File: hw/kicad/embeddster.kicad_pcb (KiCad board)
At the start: 2 copper layers, 1 part, among them U1 ESP32-DEVKIT-V1

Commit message: sch supporting tp1 & tp2
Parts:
- added C1: 100n, Capacitor_SMD:C_0805_2012Metric_Pad1.18x1.45mm_HandSolder, F.Cu at (63.0, 98.6)
- added C2: 100n, Capacitor_SMD:C_0805_2012Metric_Pad1.18x1.45mm_HandSolder, F.Cu at (63.0, 101.6)
- added D1: LED, LED_SMD:LED_0805_2012Metric_Pad1.15x1.40mm_HandSolder, F.Cu at (71.0, 96.7)
- added D2: LED, LED_SMD:LED_0805_2012Metric_Pad1.15x1.40mm_HandSolder, F.Cu at (71.0, 99.7)
- added D3: LED, LED_SMD:LED_0805_2012Metric_Pad1.15x1.40mm_HandSolder, F.Cu at (75.6, 81.2)
- added D4: LED, LED_SMD:LED_0805_2012Metric_Pad1.15x1.40mm_HandSolder, F.Cu at (75.6, 78.1)
- added D5: LED, LED_SMD:LED_0805_2012Metric_Pad1.15x1.40mm_HandSolder, F.Cu at (75.6, 75.1)
- added D6: LED, LED_SMD:LED_0805_2012Metric_Pad1.15x1.40mm_HandSolder, F.Cu at (75.6, 72.1)
- added J1: Conn_01x03_Pin, Connector_PinHeader_2.54mm:PinHeader_1x03_P2.54mm_Vertical, F.Cu at (68.4, 116.8)
- added J2: Conn_01x03_Pin, Connector_PinHeader_2.54mm:PinHeader_1x03_P2.54mm_Vertical, F.Cu at (73.1, 116.8)
- added J3: Conn_01x03_Pin, Connector_PinHeader_2.54mm:PinHeader_1x03_P2.54mm_Vertical, F.Cu at (77.7, 116.8)
- added J4: TP1_CONN, Connector_PinSocket_2.54mm:PinSocket_2x09_P2.54mm_Vertical, B.Cu at (104.6, 115.8)
- added JP1: Jumper_2_Open, TestPoint:TestPoint_2Pads_Pitch2.54mm_Drill0.8mm, F.Cu at (86.0, 115.5)
- added JP2: Jumper_2_Open, TestPoint:TestPoint_2Pads_Pitch2.54mm_Drill0.8mm, F.Cu at (127.8, 115.4)
- added R1: 680, Resistor_SMD:R_0805_2012Metric_Pad1.20x1.40mm_HandSolder, F.Cu at (75.7, 96.6)
- added R2: 470, Resistor_SMD:R_0805_2012Metric_Pad1.20x1.40mm_HandSolder, F.Cu at (75.7, 99.6)
- added R3: 220, Resistor_SMD:R_0805_2012Metric_Pad1.20x1.40mm_HandSolder, F.Cu at (80.3, 72.0)
- added R4: 220, Resistor_SMD:R_0805_2012Metric_Pad1.20x1.40mm_HandSolder, F.Cu at (80.3, 75.0)
- added R5: 220, Resistor_SMD:R_0805_2012Metric_Pad1.20x1.40mm_HandSolder, F.Cu at (80.3, 77.9)
- added R6: 220, Resistor_SMD:R_0805_2012Metric_Pad1.20x1.40mm_HandSolder, F.Cu at (80.3, 80.9)
- added U1: PLACA_CAN_V20190517, PLACA_CAN_V20190517:PLACA_CAN_V20190517, F.Cu at (155.5, 101.8)
- added U3: 74HC595, Package_SO:SOIC-16_3.9x9.9mm_P1.27mm, B.Cu at (95.5, 121.9)
- added U4: 74HC595, Package_SO:SOIC-16_3.9x9.9mm_P1.27mm, B.Cu at (116.3, 121.9)
- moved U2 54.9 mm to (134.6, 72.4), turned to 180 degrees
- renumbered U1 to U2
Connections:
- net Net-(U1-GND-Pad2) renamed GND
- U2 pad 1: unconnected-(U1-3V3-Pad1) -> Net-(JP2-A)
- U2 pad 10: unconnected-(U1-D19-Pad10) -> /CAN_MISO
- U2 pad 15: unconnected-(U1-D23-Pad15) -> /CAN_MOSI
- U2 pad 30: unconnected-(U1-VIN-Pad30) -> Net-(JP1-B)
- U2 pad 7: unconnected-(U1-TX2-Pad7) -> /CAN_nINT
- U2 pad 8: unconnected-(U1-D5-Pad8) -> /CAN_nCS
- U2 pad 9: unconnected-(U1-D18-Pad9) -> /CAN_SCK

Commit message: pcb ready for fab
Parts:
- added C3: 100n, Capacitor_SMD:C_0805_2012Metric_Pad1.18x1.45mm_HandSolder, F.Cu at (96.8, 46.2)
- added C4: 100n, Capacitor_SMD:C_0805_2012Metric_Pad1.18x1.45mm_HandSolder, B.Cu at (126.5, 87.1)
- added C5: 100n, Capacitor_SMD:C_0805_2012Metric_Pad1.18x1.45mm_HandSolder, B.Cu at (146.8, 86.9)
- added J5: Conn_01x05_Socket, Connector_PinSocket_2.54mm:PinSocket_1x05_P2.54mm_Vertical, B.Cu at (101.6, 100.1)
- added J6: Conn_01x05_Socket, Connector_PinSocket_2.54mm:PinSocket_1x05_P2.54mm_Vertical, B.Cu at (196.2, 48.2)
- added J7: Conn_01x05_Socket, Connector_PinSocket_2.54mm:PinSocket_1x05_P2.54mm_Vertical, B.Cu at (189.5, 89.4)
- added R7: 10k, Resistor_SMD:R_0805_2012Metric_Pad1.20x1.40mm_HandSolder, F.Cu at (120.7, 62.5)
- added R8: 10k, Resistor_SMD:R_0805_2012Metric_Pad1.20x1.40mm_HandSolder, B.Cu at (127.0, 69.6)
- D1: footprint LED_SMD:LED_0805_2012Metric_Pad1.15x1.40mm_HandSolder -> LED_THT:LED_D3.0mm
- R1: moved to B.Cu
- U3, U4: moved to F.Cu
- moved J3 76.8 mm to (108.5, 46.5), turned to 90 degrees
- moved C2 69.8 mm to (115.1, 55.1), turned to 180 degrees
- moved U3 63.8 mm to (108.8, 59.6), turned to 0 degrees
- moved D2 62.1 mm to (100.8, 45.2), turned to -45 degrees
- moved R2 57.0 mm to (92.7, 45.2), turned to -135 degrees
- moved C1 55.3 mm to (108.7, 67.6), turned to -45 degrees
- moved D1 48.5 mm to (117.6, 83.3), turned to 180 degrees
- moved J4 48.2 mm to (98.0, 68.1), turned to 0 degrees
- moved R1 46.9 mm to (120.7, 83.1), turned to -90 degrees
- moved U4 45.2 mm to (108.6, 77.3), turned to 0 degrees
- moved J2 43.8 mm to (105.9, 87.9), turned to 90 degrees
- moved JP1 39.8 mm to (115.1, 88.4)
- moved J1 30.3 mm to (89.6, 95.2), turned to 45 degrees
- moved JP2 23.1 mm to (117.6, 94.7), turned to 180 degrees
- moved D6 22.2 mm to (97.0, 78.0)
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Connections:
- U1 pad 2: unconnected-(U1-VIO-Pad2) -> +3V3
- U2 pad 11: unconnected-(U2-D21-Pad11) -> /TP1_RCHB
- U2 pad 14: unconnected-(U2-D22-Pad14) -> /TP1_RSWITCH
- U2 pad 21: unconnected-(U2-D32-Pad21) -> /595_SI
- U2 pad 22: unconnected-(U2-D33-Pad22) -> /595_LATCH_CLK
- U2 pad 23: unconnected-(U2-D25-Pad23) -> /595_nOE
- U2 pad 24: unconnected-(U2-D26-Pad24) -> /595_nRST
- U2 pad 25: unconnected-(U2-D27-Pad25) -> /595_SHIFT_CLK
- U2 pad 6: unconnected-(U2-RX2-Pad6) -> /TP1_RCHA
- U3 pad 1: /TP1_CSEGB -> /TP1_CSEGG
- U3 pad 15: /TP1_CSEGA -> /TP1_CSEGDP
- U3 pad 2: /TP1_CSEGC -> /TP1_CSEGF
- U3 pad 3: /TP1_CSEGD -> /TP1_CSEGE
- U3 pad 4: /TP1_CSEGE -> /TP1_CSEGD
- U3 pad 5: /TP1_CSEGF -> /TP1_CSEGC
- U3 pad 6: /TP1_CSEGG -> /TP1_CSEGB
- U3 pad 7: /TP1_CSEGDP -> /TP1_CSEGA
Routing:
- net +3V3: track 0.00 -> 233.9 mm, vias 0 -> 5
- net GND: track 0.00 -> 147.3 mm, vias 0 -> 8
- net /TP1_RCHB: track 0.00 -> 132.8 mm, vias 0 -> 3
- net +5V: track 0.00 -> 112.3 mm
- net /CAN_nCS: track 0.00 -> 101.3 mm
- net /TP1_RCHA: track 0.00 -> 98.5 mm, vias 0 -> 2
- net /TP1_RSWITCH: track 0.00 -> 96.0 mm, vias 0 -> 3
- net /CAN_MISO: track 0.00 -> 86.9 mm
- net /CAN_MOSI: track 0.00 -> 61.4 mm
- net /CAN_SCK: track 0.00 -> 51.5 mm
- net /595_LATCH_CLK: track 0.00 -> 51.3 mm, vias 0 -> 2
- net /595_SHIFT_CLK: track 0.00 -> 47.2 mm, vias 0 -> 1
- net /595_nRST: track 0.00 -> 46.5 mm, vias 0 -> 1
- net /CAN_nINT: track 0.00 -> 46.0 mm
- net /TP1_STATUS1: track 0.00 -> 39.7 mm
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- added copper zone on B.Cu, net GND
- added copper zone on F.Cu, net GND
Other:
- board outline added: 117.3 x 63 mm

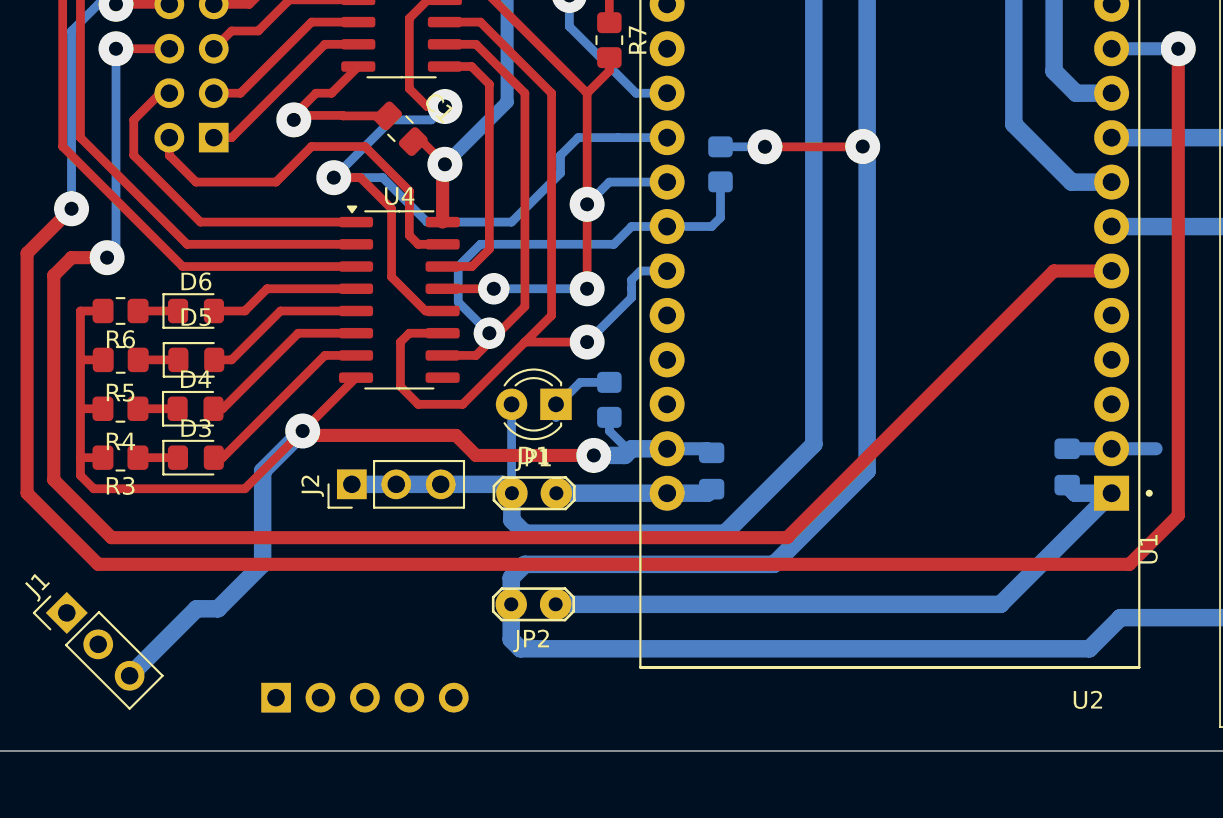
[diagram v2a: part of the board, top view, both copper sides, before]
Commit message: Add 4th quantum standoff to PCB, ground plane adjustments
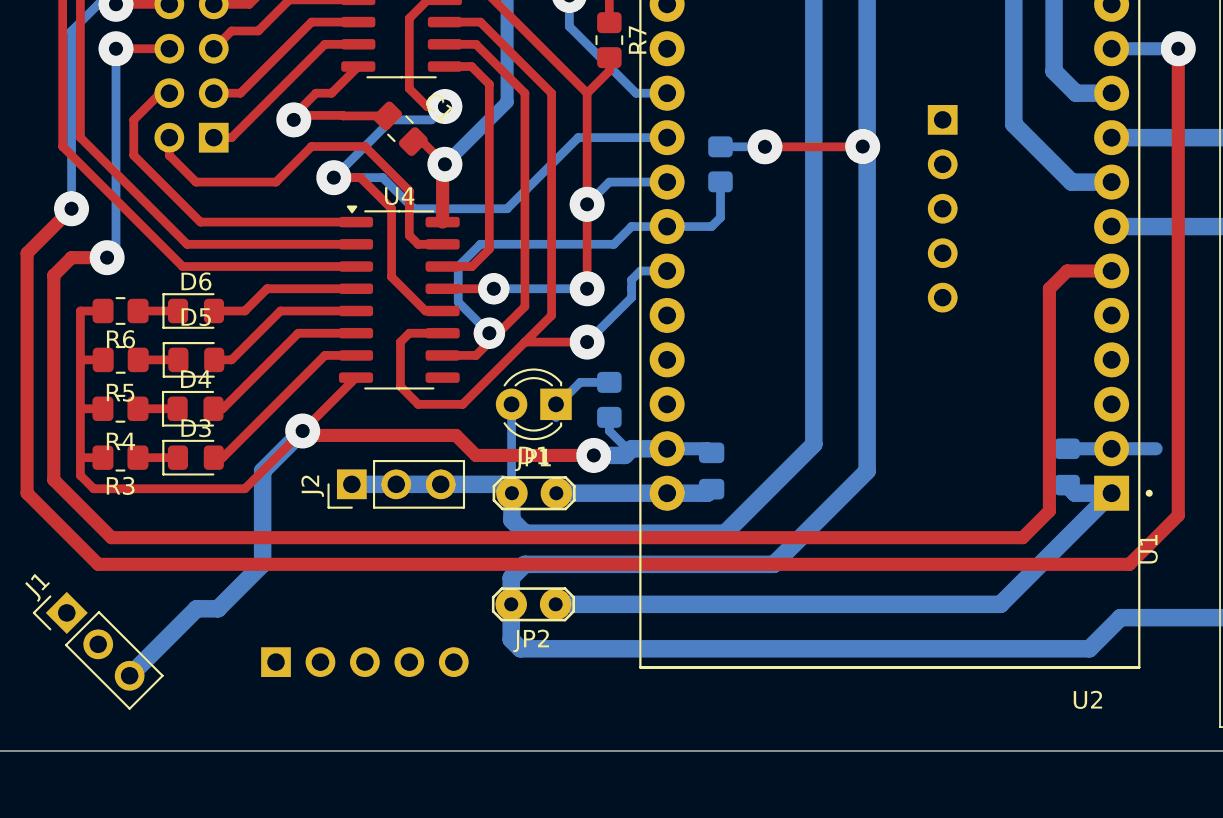
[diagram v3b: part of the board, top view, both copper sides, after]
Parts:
- added J8: Conn_01x05_Socket, Connector_PinSocket_2.54mm:PinSocket_1x05_P2.54mm_Vertical, B.Cu at (139.7, 67.1)
- moved J5 2.03 mm to (101.6, 98.0)
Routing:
- net /TP1_RCHA: track 98.5 -> 105.9 mm
- net /595_LATCH_CLK: track 51.3 -> 50.1 mm

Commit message: Add a WS2812B cell
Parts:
- added C6: 100n, Capacitor_SMD:C_0805_2012Metric_Pad1.18x1.45mm_HandSolder, F.Cu at (102.0, 87.2)
- added D7: WS2812B, LED_SMD:LED_WS2812B_PLCC4_5.0x5.0mm_P3.2mm, F.Cu at (99.3, 92.7)
- added R9: 470, Resistor_SMD:R_0805_2012Metric_Pad1.20x1.40mm_HandSolder, F.Cu at (105.2, 95.2)
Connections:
- U2 pad 11: /TP1_RCHB -> /NPXL
- U2 pad 5: unconnected-(U2-D4-Pad5) -> /TP1_RCHA
- U2 pad 6: /TP1_RCHA -> /TP1_RCHB
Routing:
- net /NPXL: track 0.00 -> 83.9 mm, vias 0 -> 1
- net +5V: track 112.3 -> 128.6 mm
- net /TP1_RCHB: track 132.8 -> 118.9 mm, vias 3 -> 2
- net GND: track 147.3 -> 160.5 mm
- net Net-(D7-DIN): track 0.00 -> 4.41 mm
- net +3V3: track 233.9 -> 236.0 mm
- net /TP1_RCHA: track 105.9 -> 103.9 mm

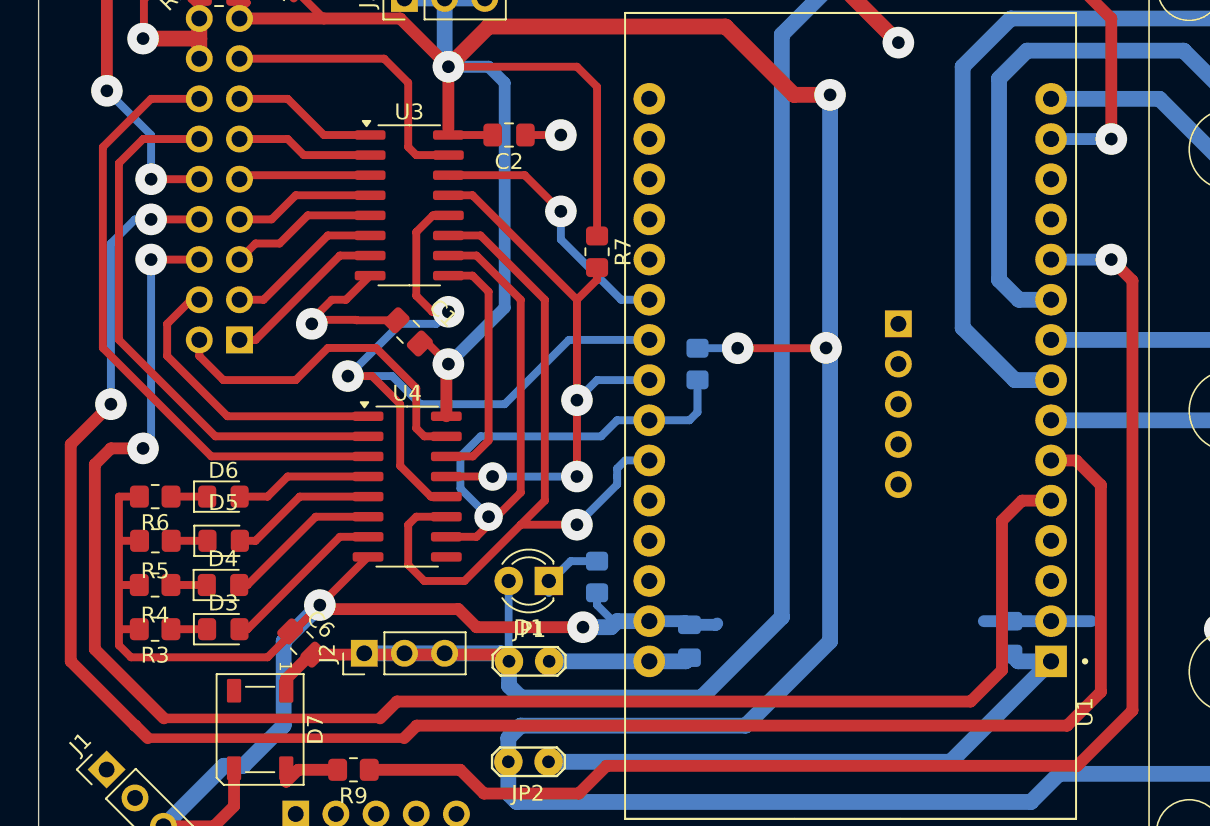
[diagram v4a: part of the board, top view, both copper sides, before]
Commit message: Fix routing, remove old pic
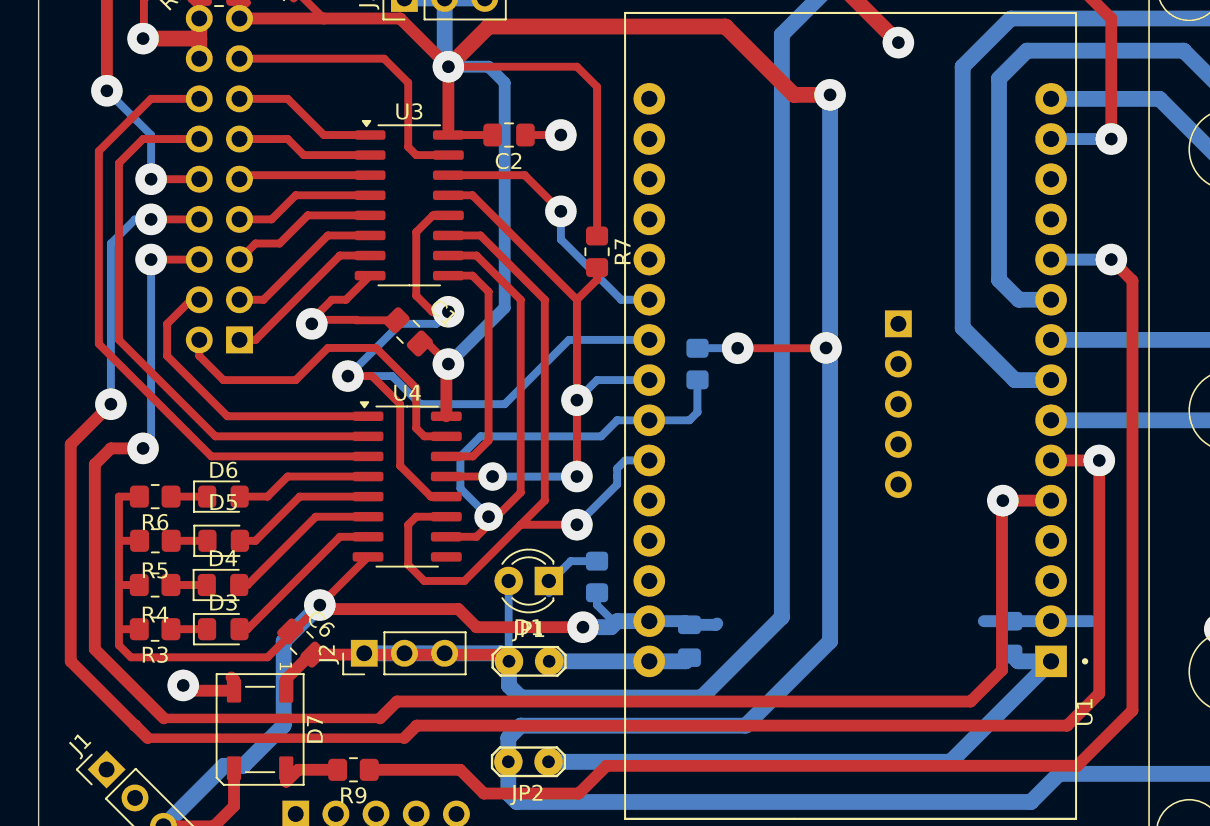
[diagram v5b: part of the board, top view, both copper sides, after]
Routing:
- net unconnected-(D7-DOUT-Pad2): track 0.00 -> 4.26 mm, vias 0 -> 1
- net /TP1_RCHB: track 118.9 -> 119.7 mm, vias 2 -> 3
- net /TP1_RCHA: track 103.9 -> 104.6 mm, vias 2 -> 3
